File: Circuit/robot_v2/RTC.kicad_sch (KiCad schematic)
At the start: 4 parts, among them J17 Molex 470531000, U11 EMC2301-1-ACZL-TR

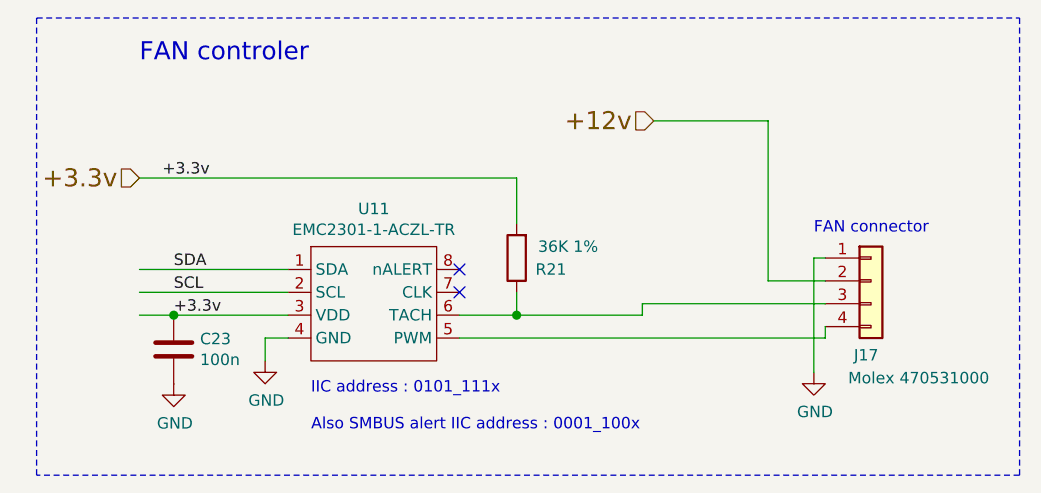
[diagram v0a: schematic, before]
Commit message: chore: Update web page and save KiCad progress
This commit includes miscellaneous updates. The project's webpage (`web/index.html`) has been modified, and various KiCad project files have been saved, reflecting ongoing design work.
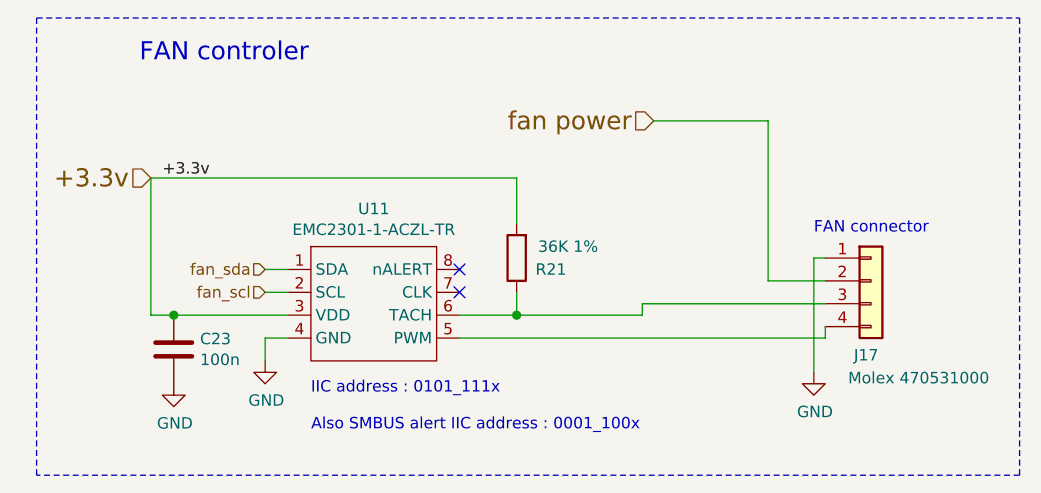
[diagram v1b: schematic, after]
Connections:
- net +12v renamed fan power
- net SCL renamed fan_scl
- net SDA renamed fan_sda
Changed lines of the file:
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@@
 	(wire
 		(pts
-			(xy 102.87 125.73) (xy 144.78 125.73)
-		)
-		(stroke
-			(width 0)
-			(type solid)
-		)
-	)
-	(wire
-		(pts
-			(xy 106.68 140.97) (xy 102.87 140.97)
+			(xy 104.14 125.73) (xy 144.78 125.73)
+		)
+		(stroke
+			(width 0)
+			(type solid)
+		)
+	)
+	(wire
+		(pts
+			(xy 106.68 140.97) (xy 104.14 140.97)
 		)
 		(stroke
@@
 	(wire
 		(pts
+			(xy 104.14 125.73) (xy 104.14 140.97)
+		)
+		(stroke
+			(width 0)
+			(type solid)
+		)
+	)
+	(wire
+		(pts
 			(xy 138.43 143.51) (xy 179.07 143.51)
 		)
@@
 	(wire
 		(pts
-			(xy 119.38 135.89) (xy 102.87 135.89)
+			(xy 119.38 135.89) (xy 116.84 135.89)
 		)
 		(stroke
@@
 	(wire
 		(pts
-			(xy 119.38 138.43) (xy 102.87 138.43)
+			(xy 119.38 138.43) (xy 116.84 138.43)
 		)
 		(stroke
@@
 		)
 	)
-	(label "SCL"
-		(at 106.68 138.43 0)
-		(fields_autoplaced yes)
-		(effects
-			(font
-				(size 1.27 1.27)
-			)
-			(justify left bottom)
-		)
-	)
-	(label "SDA"
-		(at 106.68 135.89 0)
-		(fields_autoplaced yes)
-		(effects
-			(font
-				(size 1.27 1.27)
-			)
-			(justify left bottom)
-		)
-	)
 	(label "+3.3v"
 		(at 105.41 125.73 0)
@@
 		)
 	)
-	(label "+3.3v"
-		(at 106.68 140.97 0)
+	(hierarchical_label "fan_sda"
+		(shape input)
+		(at 116.84 135.89 180)
 		(fields_autoplaced yes)
 		(effects
@@
 				(size 1.27 1.27)
 			)
-			(justify left bottom)
+			(justify right)
 		)
 	)
 	(hierarchical_label "+3.3v"
 		(shape input)
-		(at 102.87 125.73 180)
+		(at 104.14 125.73 180)
 		(fields_autoplaced yes)
 		(effects
@@
 		)
 	)
-	(hierarchical_label "+12v"
+	(hierarchical_label "fan_scl"
+		(shape input)
+		(at 116.84 138.43 180)
+		(fields_autoplaced yes)
+		(effects
+			(font
+				(size 1.27 1.27)
+			)
+			(justify right)
+		)
+	)
+	(hierarchical_label "fan power"
 		(shape input)
 		(at 160.02 119.38 180)
